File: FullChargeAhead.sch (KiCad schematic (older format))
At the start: 18 parts, among them P101 USB_OTG, P102 CONN_01X02, P103 CONN_01X02, U101 MCP73834-FCI/UN

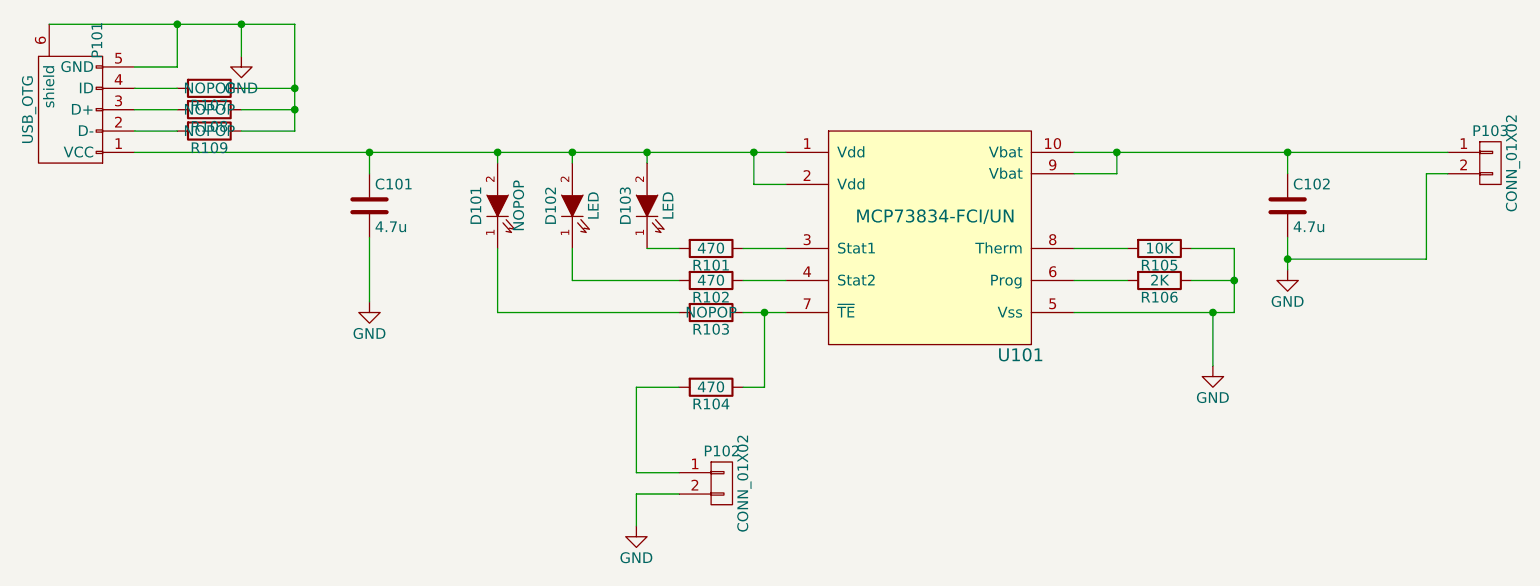
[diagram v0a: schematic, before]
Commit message: PBC finished and submitted to OSH park. Note the board is smaller than CE example and may not work as well as a result.
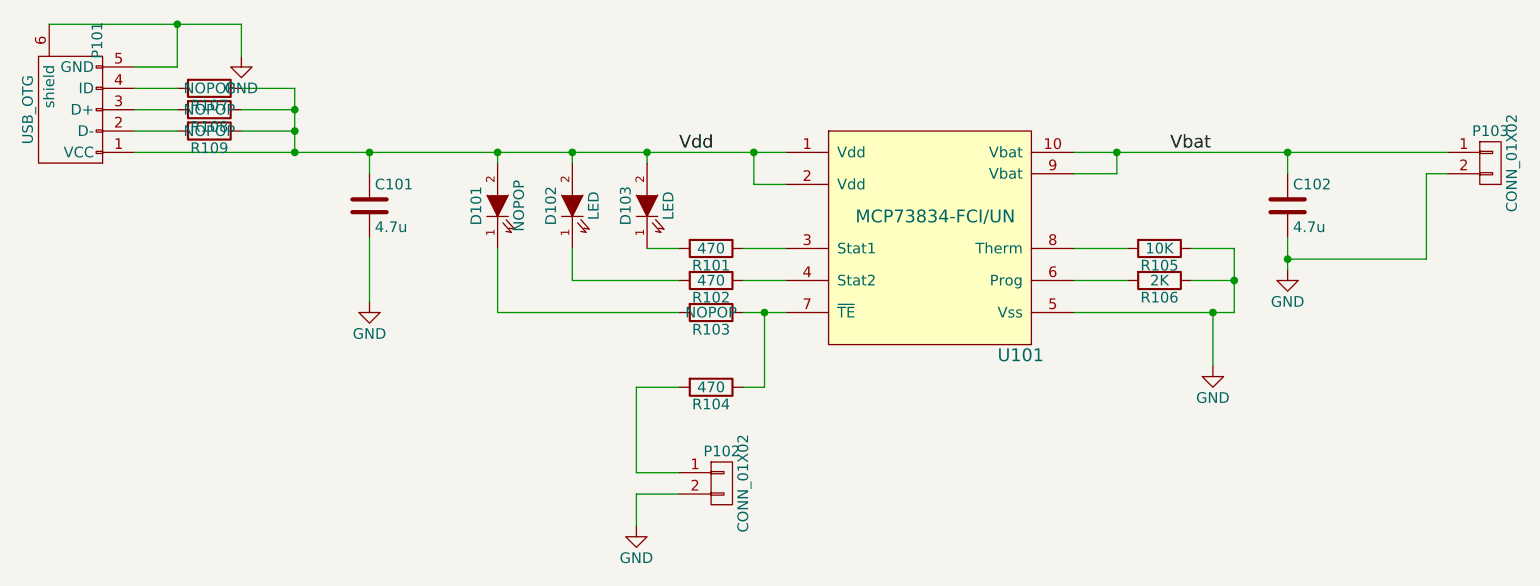
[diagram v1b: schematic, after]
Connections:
- net GND: no longer R107.1, R108.1, R109.1
- net Vdd: now reaches C101.1, D101.2 (A), D102.2 (A), D103.2 (A), P101.1 (VCC), U101.1 (Vdd), U101.2 (Vdd)
- net Vdd: now also R107.1, R108.1, R109.1
- net Vbat: now reaches C102.1, P103.1 (P1), U101.10 (Vbat), U101.9 (Vbat)
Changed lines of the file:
@@
 	3100 2800 3100 2950
-Wire Wire Line
-	2200 2800 3350 2800
 Wire Wire Line
 	2800 2800 2800 3000
@@
 	2600 3300 2800 3300
 Wire Wire Line
-	3100 3300 3350 3300
-Wire Wire Line
-	3350 3300 3350 2800
-Connection ~ 3100 2800
-Wire Wire Line
 	3100 3200 3350 3200
 Connection ~ 3350 3200
 Wire Wire Line
 	3100 3100 3350 3100
-Connection ~ 3350 3100
+Text Label 5150 3400 0    60   ~ 0
+Vdd
+Text Label 7450 3400 0    60   ~ 0
+Vbat
+Wire Wire Line
+	3100 2800 2200 2800
+Wire Wire Line
+	3350 3100 3350 3400
+Connection ~ 3350 3400
+Wire Wire Line
+	3100 3300 3350 3300
+Connection ~ 3350 3300
 $EndSCHEMATC
